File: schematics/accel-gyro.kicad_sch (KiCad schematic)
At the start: 2 parts, among them U2 LSM6DSOXTR

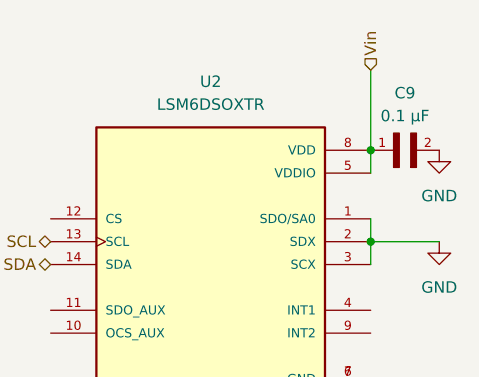
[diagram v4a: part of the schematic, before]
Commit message: 12-to-5V buck review
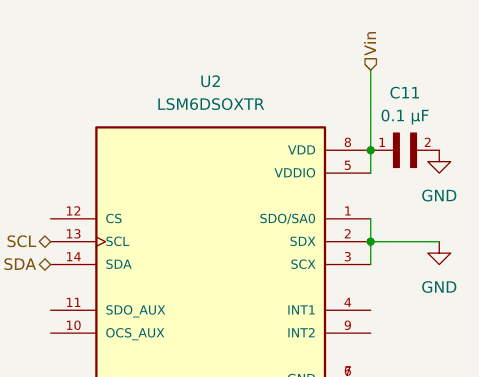
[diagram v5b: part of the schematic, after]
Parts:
- renumbered C9 to C11
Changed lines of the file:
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@@
 		(dnp no)
 		(fields_autoplaced yes)
-		(property "Reference" "C9"
+		(property "Reference" "C11"
 			(at 168.91 74.93 0)
 			(effects
@@
 			(project ""
 				(path "/2c1d9222-af16-428b-85a5-a3d420373d70/cfd34f19-b9c8-43fa-a529-56c363000dae"
-					(reference "C9")
+					(reference "C11")
 					(unit 1)
 				)
